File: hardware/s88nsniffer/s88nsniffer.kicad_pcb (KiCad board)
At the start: 2 copper layers, 78.5 x 62.5 mm, 20 parts, among them J101 RJ45, J102 RJ45, J103 Conn_01x09_Pin, J108 Conn_01x03_Pin, J109 Conn_01x02_Pin, U101 74HC14, U102 TSR_1-2490, U104 ULN2803A

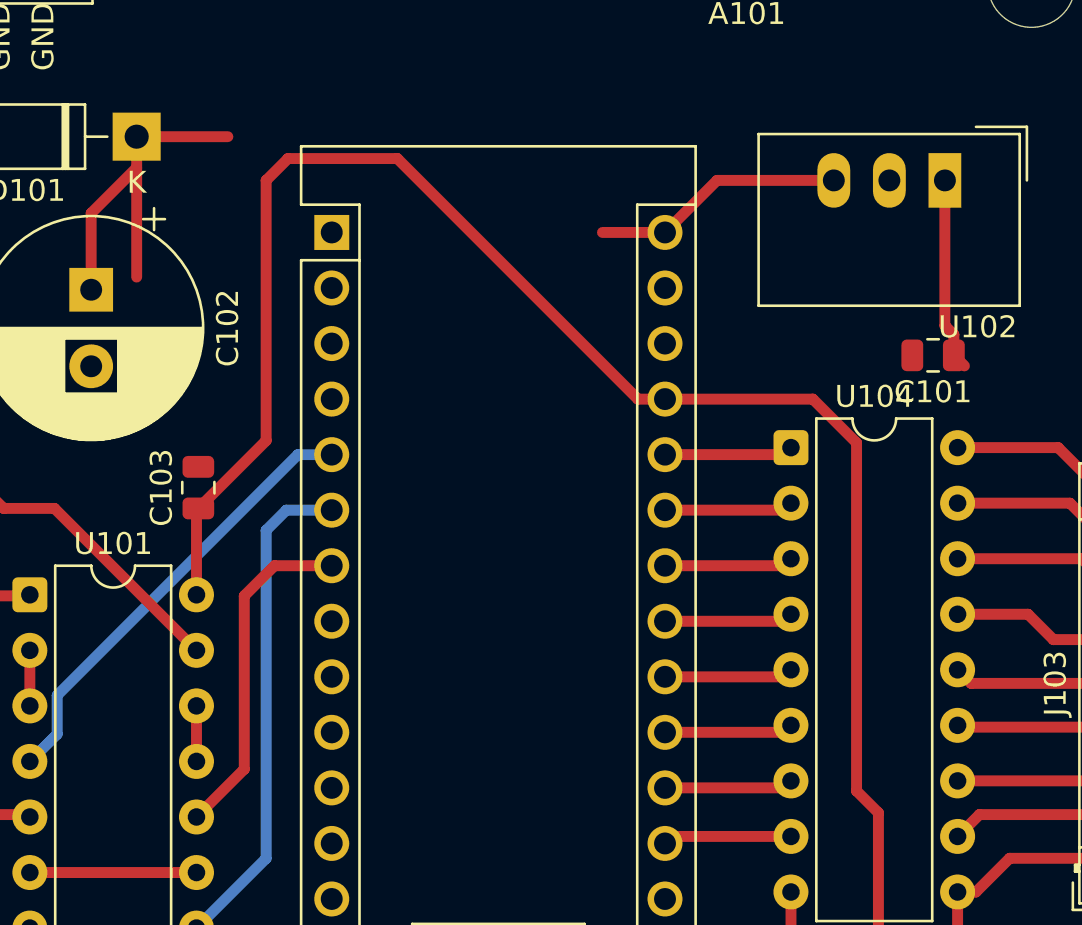
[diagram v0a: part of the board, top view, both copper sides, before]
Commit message: add component values add some info on the schematic fixed a nr of pcb layout issues
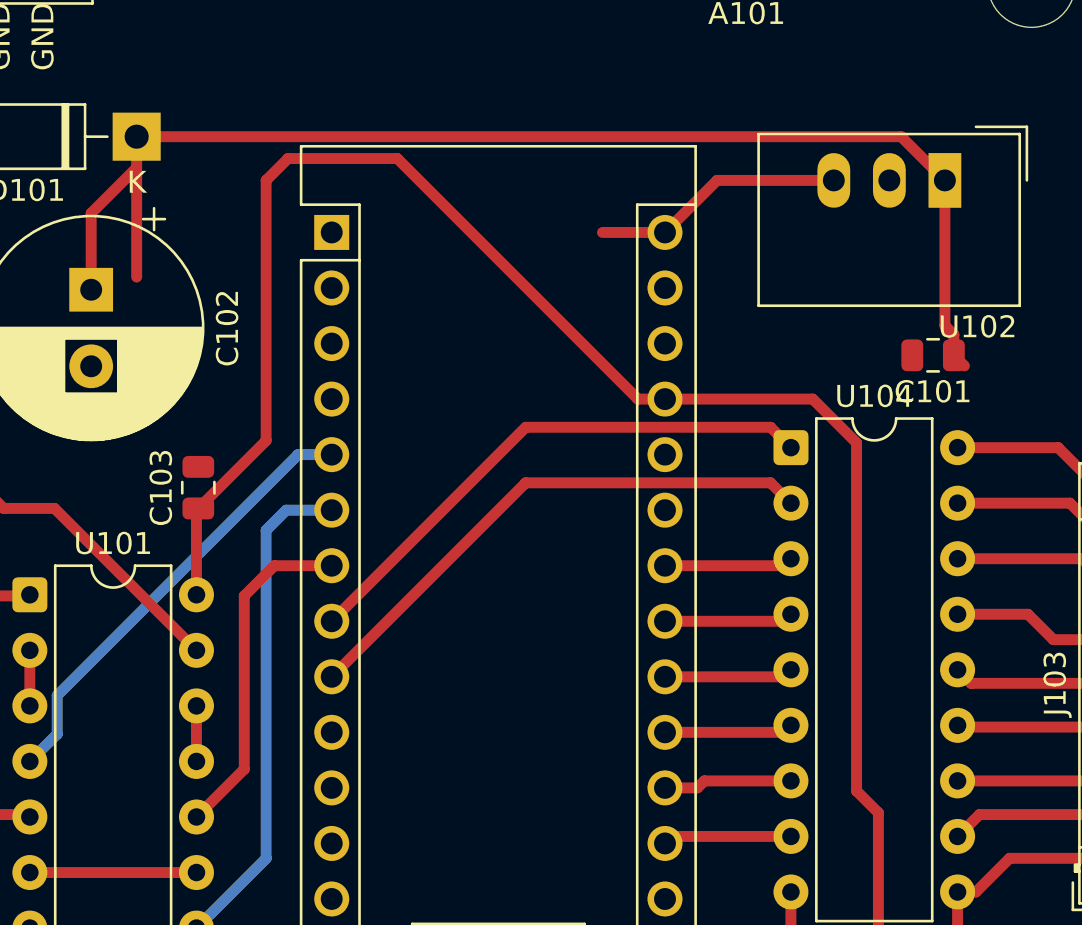
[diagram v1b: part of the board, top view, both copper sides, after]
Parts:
- C101, C103: value C -> 100n
- C102: value C_Polarized -> 470u
- R101, R102, R103: value R -> 47R
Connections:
- A101 pad 25: Net-(A101-A6) -> unconnected-(A101-A6-Pad25)
- A101 pad 26: Net-(A101-A7) -> unconnected-(A101-A7-Pad26)
- A101 pad 8: unconnected-(A101-D5-Pad8) -> Net-(A101-D5)
- A101 pad 9: unconnected-(A101-D6-Pad9) -> Net-(A101-D6)
- U104 pad 1: Net-(A101-A7) -> Net-(A101-D5)
- U104 pad 2: Net-(A101-A6) -> Net-(A101-D6)
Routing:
- net Net-(D101-K): track 25.9 -> 59.5 mm
- net Net-(A101-D6): track 0.00 -> 25.5 mm
- net Net-(A101-D5): track 0.00 -> 25.5 mm
- net Net-(A101-A7): track 5.89 -> 0.00 mm
- net Net-(A101-A6): track 5.89 -> 0.00 mm
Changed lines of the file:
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@@
 	(net 7 "unconnected-(A101-D9-Pad12)")
 	(net 8 "GND")
-	(net 9 "Net-(A101-A6)")
+	(net 9 "unconnected-(A101-A6-Pad25)")
 	(net 10 "unconnected-(A101-D12-Pad15)")
 	(net 11 "Net-(A101-A0)")
-	(net 12 "unconnected-(A101-D5-Pad8)")
+	(net 12 "Net-(A101-D5)")
 	(net 13 "Net-(A101-A4)")
 	(net 14 "+5V")
@@
 	(net 17 "unconnected-(A101-D13-Pad16)")
 	(net 18 "/data")
-	(net 19 "unconnected-(A101-D6-Pad9)")
-	(net 20 "Net-(A101-A7)")
+	(net 19 "Net-(A101-D6)")
+	(net 20 "unconnected-(A101-A7-Pad26)")
 	(net 21 "Net-(A101-A5)")
 	(net 22 "unconnected-(A101-D10-Pad13)")
@@
 			)
 		)
-		(property "Value" "C"
+		(property "Value" "100n"
 			(at 0 1.68 0)
 			(layer "F.Fab")
@@
 			)
 		)
-		(property "Value" "R"
+		(property "Value" "47R"
 			(at 0 1.68 0)
 			(layer "F.Fab")
@@
 			(layers "*.Cu" "*.Mask")
 			(remove_unused_layers no)
-			(net 12 "unconnected-(A101-D5-Pad8)")
+			(net 12 "Net-(A101-D5)")
 			(pinfunction "D5")
-			(pintype "bidirectional+no_connect")
+			(pintype "bidirectional")
 		)
 		(pad "9" thru_hole oval
@@
 			(layers "*.Cu" "*.Mask")
 			(remove_unused_layers no)
-			(net 19 "unconnected-(A101-D6-Pad9)")
+			(net 19 "Net-(A101-D6)")
 			(pinfunction "D6")
-			(pintype "bidirectional+no_connect")
+			(pintype "bidirectional")
 		)
 		(pad "10" thru_hole oval
@@
 			(layers "*.Cu" "*.Mask")
 			(remove_unused_layers no)
-			(net 9 "Net-(A101-A6)")
+			(net 9 "unconnected-(A101-A6-Pad25)")
 			(pinfunction "A6")
 			(pintype "bidirectional")
@@
 			(layers "*.Cu" "*.Mask")
 			(remove_unused_layers no)
-			(net 20 "Net-(A101-A7)")
+			(net 20 "unconnected-(A101-A7-Pad26)")
 			(pinfunction "A7")
 			(pintype "bidirectional")
@@
 			)
 		)
-		(property "Value" "C"
+		(property "Value" "100n"
 			(at 0 1.68 90)
 			(layer "F.Fab")
@@
 			)
 		)
-		(property "Value" "R"
+		(property "Value" "47R"
 			(at 0 1.68 0)
 			(layer "F.Fab")
@@
 			)
 		)
-		(property "Value" "C_Polarized"
+		(property "Value" "470u"
 			(at 1.75 6.25 90)
 			(layer "F.Fab")
@@
 			)
 		)
-		(property "Value" "R"
+		(property "Value" "47R"
 			(at 0 1.68 0)
 			(layer "F.Fab")
@@
 			(remove_unused_layers no)
 			(roundrect_rratio 0.15625)
-			(net 20 "Net-(A101-A7)")
+			(net 12 "Net-(A101-D5)")
 			(pinfunction "I1")
 			(pintype "input")
@@
 			(layers "*.Cu" "*.Mask")
 			(remove_unused_layers no)
-			(net 9 "Net-(A101-A6)")
+			(net 19 "Net-(A101-D6)")
 			(pinfunction "I2")
 			(pintype "input")
@@
 	(segment
 		(start 137.24 92.78)
-		(end 142.68 92.78)
+		(end 138.72 92.78)
 		(width 0.5)
 		(layer "F.Cu")
@@
 	)
 	(segment
-		(start 142.68 92.78)
+		(start 139.04 92.46)
 		(end 143 92.46)
 		(width 0.5)
@@
 	)
 	(segment
+		(start 138.72 92.78)
+		(end 139.04 92.46)
+		(width 0.5)
+		(layer "F.Cu")
+		(net 6)
+	)
+	(segment
 		(start 143 103)
 		(end 137 109)
@@
 	)
 	(segment
-		(start 142.68 80.08)
-		(end 143 79.76)
+		(start 143 95)
+		(end 137.56 95)
 		(width 0.5)
 		(layer "F.Cu")
-		(net 9)
+		(net 11)
 	)
 	(segment
-		(start 137.24 80.08)
-		(end 142.68 80.08)
+		(start 137.56 95)
+		(end 137.24 95.32)
 		(width 0.5)
 		(layer "F.Cu")
-		(net 9)
+		(net 11)
 	)
 	(segment
-		(start 137.56 95)
-		(end 137.24 95.32)
+		(start 130.871 76.289)
+		(end 122 85.16)
 		(width 0.5)
 		(layer "F.Cu")
-		(net 11)
+		(net 12)
 	)
 	(segment
-		(start 143 95)
-		(end 137.56 95)
+		(start 142.68 77.54)
+		(end 143 77.22)
 		(width 0.5)
 		(layer "F.Cu")
-		(net 11)
+		(net 12)
+	)
+	(segment
+		(start 142.069 76.289)
+		(end 130.871 76.289)
+		(width 0.5)
+		(layer "F.Cu")
+		(net 12)
+	)
+	(segment
+		(start 143 77.22)
+		(end 142.069 76.289)
+		(width 0.5)
+		(layer "F.Cu")
+		(net 12)
 	)
 	(segment
@@
 	)
 	(segment
-		(start 142.68 77.54)
-		(end 143 77.22)
+		(start 142.069 78.829)
+		(end 130.871 78.829)
+		(width 0.5)
+		(layer "F.Cu")
+		(net 19)
+	)
+	(segment
+		(start 130.871 78.829)
+		(end 122 87.7)
 		(width 0.5)
 		(layer "F.Cu")
-		(net 20)
+		(net 19)
 	)
 	(segment
-		(start 137.24 77.54)
-		(end 142.68 77.54)
+		(start 142.68 80.08)
+		(end 143 79.76)
+		(width 0.5)
+		(layer "F.Cu")
+		(net 19)
+	)
+	(segment
+		(start 143 79.76)
+		(end 142.069 78.829)
 		(width 0.5)
 		(layer "F.Cu")
-		(net 20)
+		(net 19)
 	)
 	(segment
@@
 	)
 	(segment
+		(start 113.08 63)
+		(end 148.04 63)
+		(width 0.5)
+		(layer "F.Cu")
+		(net 30)
+	)
+	(segment
+		(start 148.04 63)
+		(end 150.04 65)
+		(width 0.5)
+		(layer "F.Cu")
+		(net 30)
+	)
+	(segment
 		(start 111 66.5)
 		(end 113.08 64.42)
@@
 		(width 0.5)
 		(layer "F.Cu")
-		(net 30)
-	)
-	(segment
-		(start 113.08 63)
-		(end 117.25 63)
-		(width 0.5)
-		(layer "F.Cu")
